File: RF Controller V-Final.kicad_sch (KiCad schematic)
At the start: 36 parts, among them J2 J_OLED, J3 BAT+, J4 BAT-, SW1 EG1218, U1 Teensy4.0, U3 NRF24L01, U5 AP2112K-3.3, U7 Pitch/Roll, U8 TPS542025DDCR, U9 Throttle/Yaw

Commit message: OLED display update
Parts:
- C1: value TBD -> 0.1u
- R1, R2: value TBD -> 4.7k
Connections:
- net 3.3V_OUT: now also C1.1, J2.2 (Pin_2), R1.1, R2.2
- net GND: now also C1.2, J2.1 (Pin_1)
- net SCL: now reaches R1.2
- net SCL: now also J2.3 (Pin_3)
- net SDA: now reaches R2.1
- net SDA: now also J2.4 (Pin_4)
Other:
- moved on the sheet: C1, R1, R2

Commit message: OLED Update V2
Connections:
- net SCL: now also U1.26 (19_A5_SCL0)
- net SDA: now also U1.25 (18_A4_SDA0)
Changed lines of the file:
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@@
+		)
+	)
+	(wire
+		(pts
+			(xy 35.56 179.07) (xy 36.83 179.07)
+		)
+		(stroke
+			(width 0)
+			(type default)
 		)
 	)
@@
 			(width 0)
 			(type dash)
+		)
+	)
+	(wire
+		(pts
+			(xy 35.56 181.61) (xy 36.83 181.61)
+		)
+		(stroke
+			(width 0)
+			(type default)
 		)
 	)
@@
 		)
 	)
+	(label "SDA"
+		(at 35.56 179.07 180)
+		(effects
+			(font
+				(size 1.27 1.27)
+			)
+			(justify right bottom)
+		)
+	)
 	(label "3.3V_OUT"
 		(at 238.76 58.42 180)
@@
 		(effects
 			(font
+				(size 1.27 1.27)
+			)
+			(justify right bottom)
+		)
+	)
+	(label "SCL"
+		(at 35.56 181.61 180)
+		(effects
+			(font

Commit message: RF Link upd and other pins
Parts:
- R3: value TBD -> 330
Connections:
- net ADC_IN is gone; now on net ADC7: C13.1, R4.1, R5.1
- net GND: now also D7.1 (K)
- net ADC6: now reaches R3.1
- net ADC6: now also U1.27 (20_A6_TX5_LRCLK1)
- net ADC7: now reaches U1.28 (21_A7_RX5_BCLK1)
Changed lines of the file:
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@@
+		)
+	)
+	(label "ADC6"
+		(at 36.83 184.15 180)
+		(effects
+			(font
+				(size 1.27 1.27)
+			)
+			(justify right bottom)
 		)
 	)
@@
 		)
 	)
+	(label "ADC6"
+		(at 114.3 58.42 180)
+		(effects
+			(font
+				(size 1.27 1.27)
+			)
+			(justify right bottom)
+		)
+	)
 	(label "3.3V_OUT"
 		(at 196.85 57.15 180)
@@
 		)
 	)
+	(label "ADC7"
+		(at 36.83 186.69 180)
+		(effects
+			(font
+				(size 1.27 1.27)
+			)
+			(justify right bottom)
+		)
+	)
 	(label "MISO"
 		(at 35.56 151.13 180)
@@
 		)
 	)
-	(label "ADC_IN"
+	(label "ADC7"
 		(at 133.35 88.9 0)
 		(effects
@@
 	)
 	(symbol
+		(lib_id "power:GND")
+		(at 132.08 58.42 90)
+		(unit 1)
+		(body_style 1)
+		(exclude_from_sim no)
+		(in_bom yes)
+		(on_board yes)
+		(in_pos_files yes)
+		(dnp no)
+		(fields_autoplaced yes)
+		(property "Reference" "#PWR025"
+			(at 138.43 58.42 0)
+			(hide yes)
+			(show_name no)
+			(do_not_autoplace no)
+			(effects
+				(font
+					(size 1.27 1.27)
+				)
+			)
+		)
+		(property "Value" "GND"
+			(at 135.89 58.4199 90)
+			(show_name no)
+			(do_not_autoplace no)
+			(effects
+				(font
+					(size 1.27 1.27)
+				)
+				(justify right)
+			)
+		)
+		(property "Footprint" ""
+			(at 132.08 58.42 0)
+			(hide yes)
+			(show_name no)
+			(do_not_autoplace no)
+			(effects
+				(font
+					(size 1.27 1.27)
+				)
+			)
+		)
+		(property "Datasheet" ""
+			(at 132.08 58.42 0)
+			(hide yes)
+			(show_name no)
+			(do_not_autoplace no)
+			(effects
+				(font
+					(size 1.27 1.27)
+				)
+			)
+		)
+		(property "Description" "Power symbol creates a global label with name \"GND\" , ground"
+			(at 132.08 58.42 0)
+			(hide yes)
+			(show_name no)
+			(do_not_autoplace no)
+			(effects
+				(font
+					(size 1.27 1.27)
+				)
+			)
+		)
+		(pin "1"
+		)
+		(instances
+			(project "RF Controller V-Final"
+				(path "/20b51a64-697d-4081-9410-2d5c496e59fa"
+					(reference "#PWR025")
+					(unit 1)
+				)
+			)
+		)
+	)
+	(symbol
 		(lib_id "Pads:_1")
 		(at 24.13 30.48 0)
@@
 			)
 		)
-		(property "Value" "TBD"
+		(property "Value" "330"
 			(at 119.634 56.134 90)
 			(show_name no)

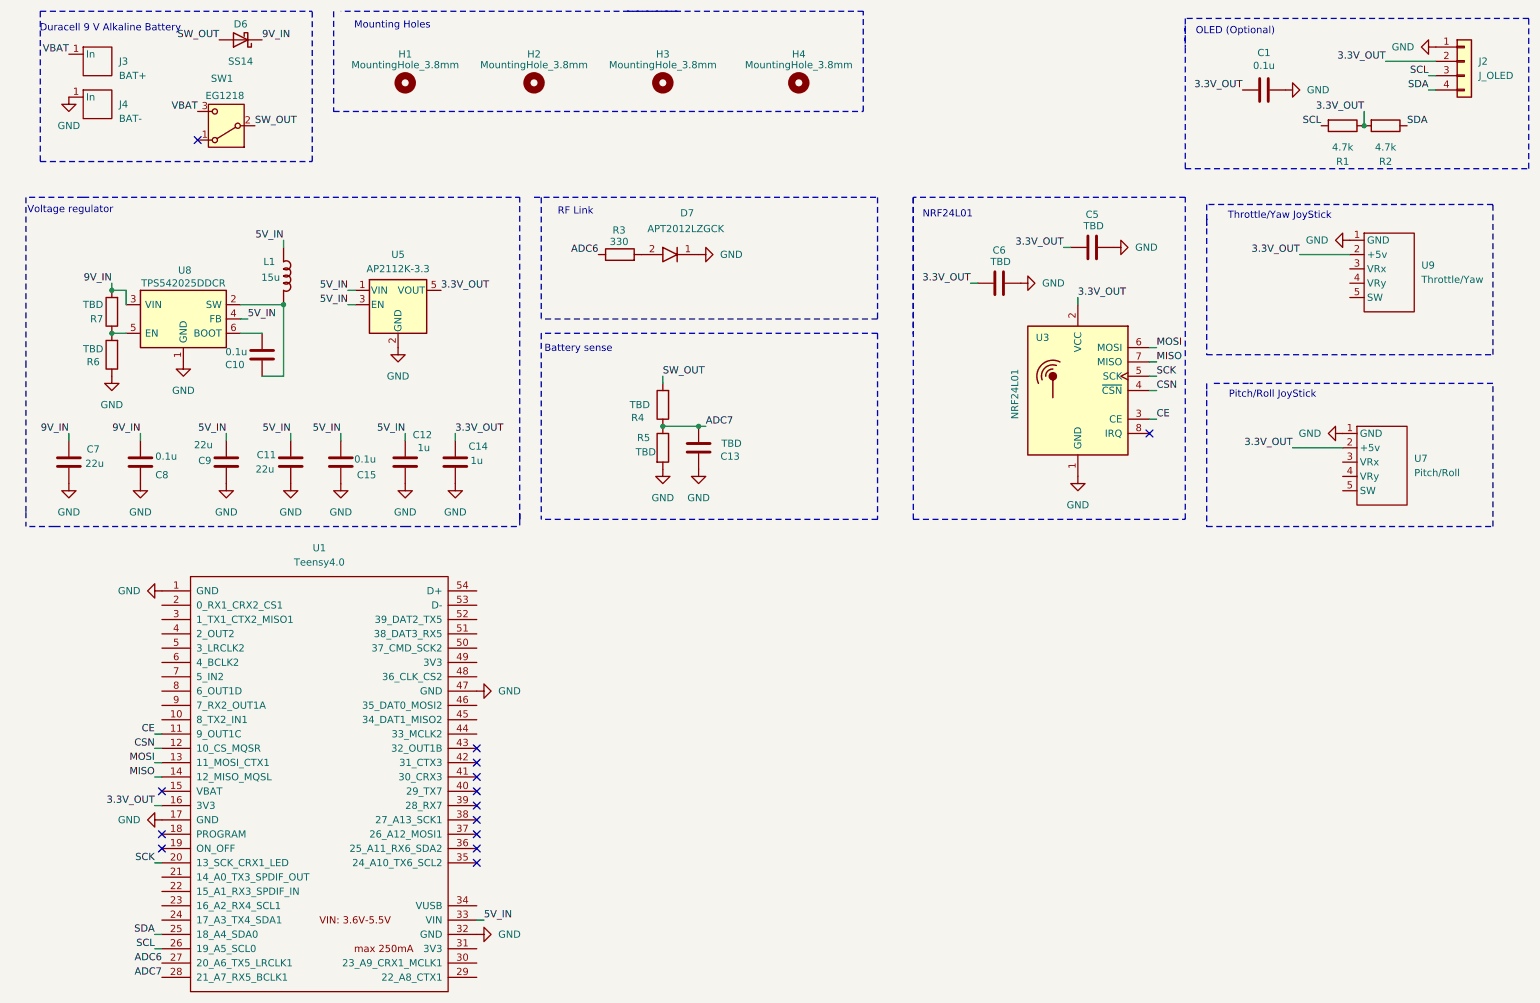
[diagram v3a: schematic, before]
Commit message: Component values V1
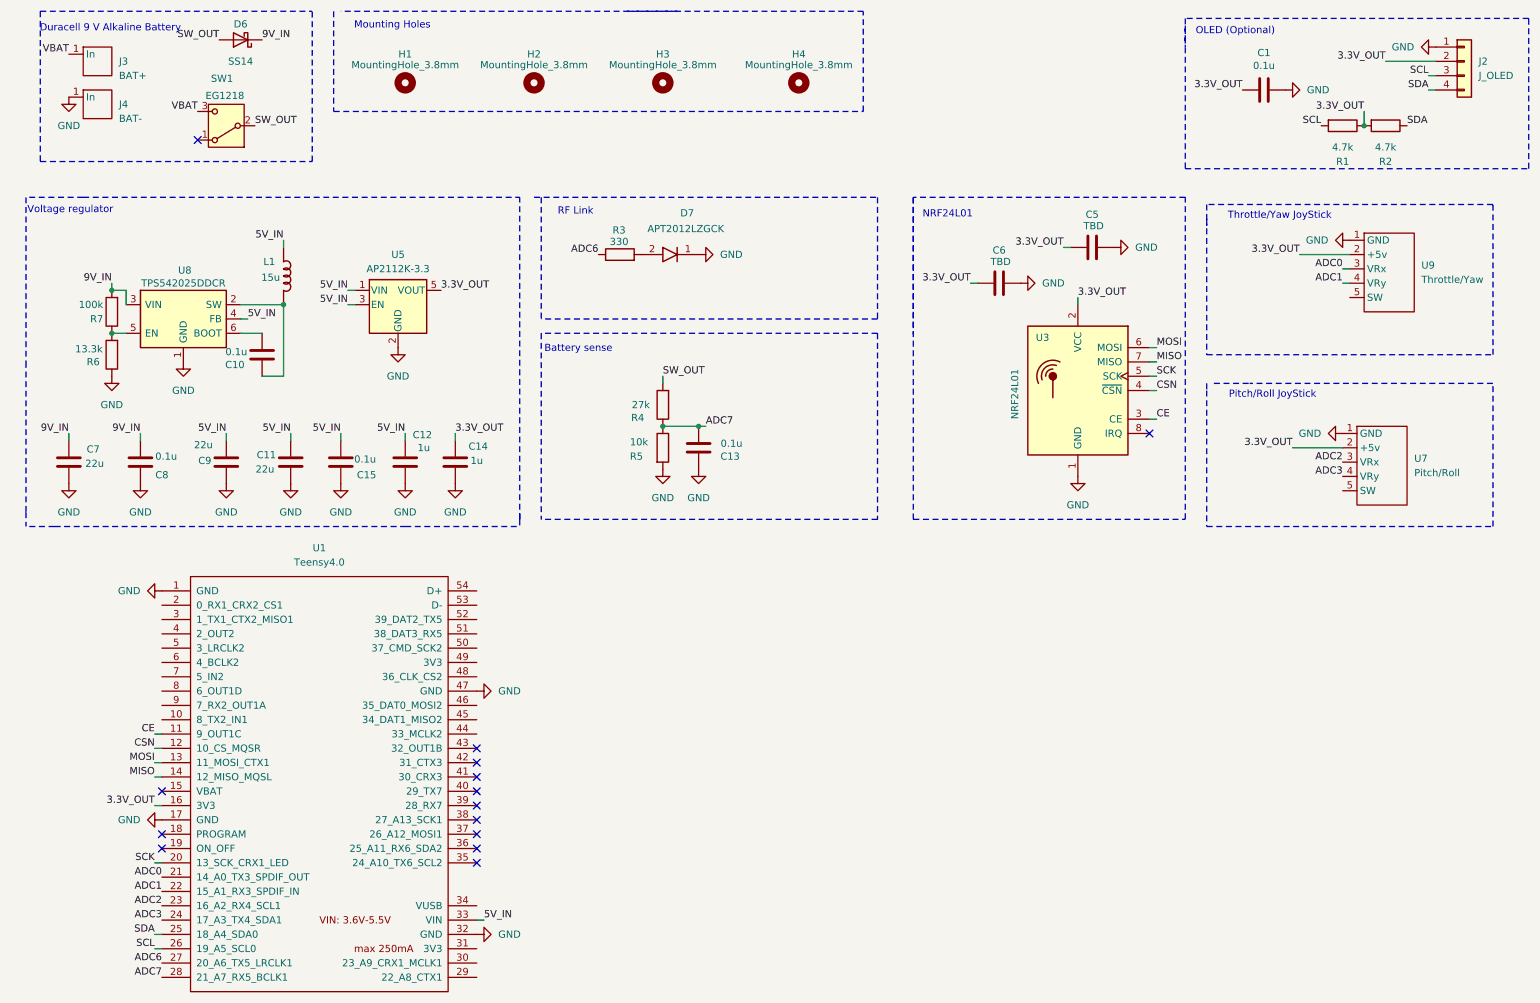
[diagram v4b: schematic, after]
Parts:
- C13: value TBD -> 0.1u
- R4: value TBD -> 27k
- R5: value TBD -> 10k
- R6: value TBD -> 13.3k
- R7: value TBD -> 100k
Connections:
- net ADC0: now reaches U9.3 (VRx)
- net ADC0: now also U1.21 (14_A0_TX3_SPDIF_OUT)
- net ADC1: now reaches U9.4 (VRy)
- net ADC1: now also U1.22 (15_A1_RX3_SPDIF_IN)
- net ADC2: now reaches U7.3 (VRx)
- net ADC2: now also U1.23 (16_A2_RX4_SCL1)
- net ADC3: now reaches U7.4 (VRy)
- net ADC3: now also U1.24 (17_A3_TX4_SDA1)
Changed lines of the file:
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@@
 	(wire
 		(pts
+			(xy 246.38 60.96) (xy 247.65 60.96)
+		)
+		(stroke
+			(width 0)
+			(type default)
+		)
+	)
+	(wire
+		(pts
 			(xy 33.02 90.17) (xy 33.02 91.44)
 		)
@@
 	(wire
 		(pts
+			(xy 246.38 63.5) (xy 247.65 63.5)
+		)
+		(stroke
+			(width 0)
+			(type default)
+		)
+	)
+	(wire
+		(pts
 			(xy 132.08 88.9) (xy 133.35 88.9)
 		)
@@
 		)
 	)
+	(label "ADC0"
+		(at 246.38 60.96 180)
+		(effects
+			(font
+				(size 1.27 1.27)
+			)
+			(justify right bottom)
+		)
+	)
 	(label "SDA"
 		(at 261.62 29.21 180)
@@
 		)
 	)
+	(label "ADC3"
+		(at 246.38 97.79 180)
+		(effects
+			(font
+				(size 1.27 1.27)
+			)
+			(justify right bottom)
+		)
+	)
 	(label "9V_IN"
 		(at 33.02 90.17 180)
@@
 		)
 	)
+	(label "ADC2"
+		(at 36.83 173.99 180)
+		(effects
+			(font
+				(size 1.27 1.27)
+			)
+			(justify right bottom)
+		)
+	)
+	(label "ADC1"
+		(at 36.83 171.45 180)
+		(effects
+			(font
+				(size 1.27 1.27)
+			)
+			(justify right bottom)
+		)
+	)
 	(label "3.3V_OUT"
 		(at 196.85 57.15 180)
@@
 		)
 	)
+	(label "ADC2"
+		(at 246.38 95.25 180)
+		(effects
+			(font
+				(size 1.27 1.27)
+			)
+			(justify right bottom)
+		)
+	)
 	(label "3.3V_OUT"
 		(at 228.6 29.21 180)
@@
 		)
 	)
+	(label "ADC1"
+		(at 246.38 63.5 180)
+		(effects
+			(font
+				(size 1.27 1.27)
+			)
+			(justify right bottom)
+		)
+	)
+	(label "ADC0"
+		(at 36.83 168.91 180)
+		(effects
+			(font
+				(size 1.27 1.27)
+			)
+			(justify right bottom)
+		)
+	)
 	(label "CE"
 		(at 35.56 143.51 180)
@@
 		)
 	)
+	(label "ADC3"
+		(at 36.83 176.53 180)
+		(effects
+			(font
+				(size 1.27 1.27)
+			)
+			(justify right bottom)
+		)
+	)
 	(label "SCK"
 		(at 35.56 166.37 180)
@@
 			)
 		)
-		(property "Value" "TBD"
+		(property "Value" "27k"
 			(at 123.444 85.09 0)
 			(show_name no)
@@
 			)
 		)
-		(property "Value" "TBD"
-			(at 24.638 75.184 0)
+		(property "Value" "13.3k"
+			(at 23.876 75.184 0)
 			(show_name no)
 			(do_not_autoplace no)
@@
 			)
 		)
-		(property "Value" "TBD"
+		(property "Value" "100k"
 			(at 26.416 67.31 0)
 			(show_name no)
@@
 			)
 		)
-		(property "Value" "TBD"
+		(property "Value" "0.1u"
 			(at 137.922 91.948 0)
 			(show_name no)
@@
 		(dnp no)
 		(property "Reference" "R5"
-			(at 121.158 90.932 0)
+			(at 119.888 94.234 0)
 			(show_name no)
 			(do_not_autoplace no)
@@
 			)
 		)
-		(property "Value" "TBD"
-			(at 120.904 93.472 0)
+		(property "Value" "10k"
+			(at 119.888 91.694 0)
 			(show_name no)
 			(do_not_autoplace no)

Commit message: Component values V2
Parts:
- C5: value TBD -> 10u
- C6: value TBD -> 0.1u
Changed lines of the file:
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@@
 			)
 		)
-		(property "Value" "TBD"
+		(property "Value" "0.1u"
 			(at 185.674 59.69 90)
 			(show_name no)
@@
 			)
 		)
-		(property "Value" "TBD"
+		(property "Value" "10u"
 			(at 202.184 53.34 90)
 			(show_name no)
